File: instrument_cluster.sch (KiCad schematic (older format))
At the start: 2 parts

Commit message: finish scheme & change libs path
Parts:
- removed J?: Conn_02x16_Top_Bottom, symbol Conn_02x16_Top_Bottom
- added J1: Conn_02x16_Top_Bottom, Kulibin:Pin_Header_Angled_2x16_Pitch2.54mm, symbol Conn_02x16_Top_Bottom
- gave numbers to parts that had none: 1
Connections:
- net labels added: +3V3_A, +3V3_B, +5V_A, +5V_B, FUEL_TANK_in, FUEL_TANK_out1, FUEL_TANK_out2, LIN_(contact_spiral), LIN_+12V, USB_Vbus_A, USB_Vbus_B
- net labels removed: FUEL_TANK_in1, FUEL_TANK_in2, FUEL_TANK_out, SPIRAL
- wire segments 39 -> 78
- no-connect marks 2 -> 33
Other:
- note added: "two separate module on 1 PCB\n- module B powered from Vbatt\n- module A powered from IGN\n(Vbatt present always)"
- note removed: "two separate module on 1 PCB\n- module B power from Vbatt\n- module A power from IGN\n(Vbatt present always)"
- moved on the sheet: J2

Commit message: specify footpints to resistors and capasitors
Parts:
- J1: footprint Kulibin:Pin_Header_Angled_2x16_Pitch2.54mm -> zulljon:Pin_Header_Angled_2x16_Pitch2.54mm
- J2: footprint (none) -> zulljon:Socket_Strip_Straight_2x16_Pitch2.54mm
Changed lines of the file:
@@
 F 0 "J2" H 9500 2800 50  0000 C CNN
 F 1 "Conn_02x16_Top_Bottom" H 9500 1100 50  0000 C CNN
-F 2 "" H 9450 2000 50  0001 C CNN
+F 2 "zulljon:Socket_Strip_Straight_2x16_Pitch2.54mm" H 9450 2000 50  0001 C CNN
 F 3 "" H 9450 2000 50  0001 C CNN
 	1    9450 2000
@@
 	5750 3900 5750 4000
 $Comp
-L GND #PWR01
+L GND #PWR3
 U 1 1 5A075102
 P 5750 4000
-F 0 "#PWR01" H 5750 3750 50  0001 C CNN
+F 0 "#PWR3" H 5750 3750 50  0001 C CNN
 F 1 "GND" H 5750 3850 50  0000 C CNN
 F 2 "" H 5750 4000 50  0001 C CNN
@@
 $EndComp
 $Comp
-L GND #PWR02
+L GND #PWR1
 U 1 1 5A0766C2
 P 1000 7500
-F 0 "#PWR02" H 1000 7250 50  0001 C CNN
+F 0 "#PWR1" H 1000 7250 50  0001 C CNN
 F 1 "GND" H 1150 7450 50  0000 C CNN
 F 2 "" H 1000 7500 50  0001 C CNN
@@
 	5800 2350 5800 2450
 $Comp
-L GND #PWR03
+L GND #PWR4
 U 1 1 5A0B0A63
 P 5800 2450
-F 0 "#PWR03" H 5800 2200 50  0001 C CNN
+F 0 "#PWR4" H 5800 2200 50  0001 C CNN
 F 1 "GND" H 5800 2300 50  0000 C CNN
 F 2 "" H 5800 2450 50  0001 C CNN
@@
 	2250 3950 2250 4050
 $Comp
-L GND #PWR04
+L GND #PWR2
 U 1 1 5A0C0519
 P 2250 4050
-F 0 "#PWR04" H 2250 3800 50  0001 C CNN
+F 0 "#PWR2" H 2250 3800 50  0001 C CNN
 F 1 "GND" H 2250 3900 50  0000 C CNN
 F 2 "" H 2250 4050 50  0001 C CNN
@@
 F 0 "J1" H 2400 5450 50  0000 C CNN
 F 1 "Conn_02x16_Top_Bottom" H 2400 5550 50  0000 C CNN
-F 2 "Kulibin:Pin_Header_Angled_2x16_Pitch2.54mm" H 2350 6550 50  0001 C CNN
+F 2 "zulljon:Pin_Header_Angled_2x16_Pitch2.54mm" H 2350 6550 50  0001 C CNN
 F 3 "" H 2350 6550 50  0001 C CNN
 	1    2350 6550

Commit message: add missed footprints, add additional capasitors on 3.3V line, fix banch of ERC errors
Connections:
- no-connect marks 33 -> 34
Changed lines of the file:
@@
 	5750 3900 5750 4000
 $Comp
-L GND #PWR3
+L GND #PWR01
 U 1 1 5A075102
 P 5750 4000
-F 0 "#PWR3" H 5750 3750 50  0001 C CNN
+F 0 "#PWR01" H 5750 3750 50  0001 C CNN
 F 1 "GND" H 5750 3850 50  0000 C CNN
 F 2 "" H 5750 4000 50  0001 C CNN
@@
 $EndComp
 $Comp
-L GND #PWR1
+L GND #PWR02
 U 1 1 5A0766C2
-P 1000 7500
-F 0 "#PWR1" H 1000 7250 50  0001 C CNN
-F 1 "GND" H 1150 7450 50  0000 C CNN
-F 2 "" H 1000 7500 50  0001 C CNN
-F 3 "" H 1000 7500 50  0001 C CNN
-	1    1000 7500
+P 1300 7550
+F 0 "#PWR02" H 1300 7300 50  0001 C CNN
+F 1 "GND" H 1450 7500 50  0000 C CNN
+F 2 "" H 1300 7550 50  0001 C CNN
+F 3 "" H 1300 7550 50  0001 C CNN
+	1    1300 7550
 	1    0    0    -1
 $EndComp
@@
 	850  7400 950  7500
 Wire Wire Line
-	950  7500 1000 7500
+	950  7500 1300 7500
 Wire Bus Line
 	850  700  850  7400
@@
 	5800 2350 5800 2450
 $Comp
-L GND #PWR4
+L GND #PWR03
 U 1 1 5A0B0A63
 P 5800 2450
-F 0 "#PWR4" H 5800 2200 50  0001 C CNN
+F 0 "#PWR03" H 5800 2200 50  0001 C CNN
 F 1 "GND" H 5800 2300 50  0000 C CNN
 F 2 "" H 5800 2450 50  0001 C CNN
@@
 	2250 3950 2250 4050
 $Comp
-L GND #PWR2
+L GND #PWR04
 U 1 1 5A0C0519
 P 2250 4050
-F 0 "#PWR2" H 2250 3800 50  0001 C CNN
+F 0 "#PWR04" H 2250 3800 50  0001 C CNN
 F 1 "GND" H 2250 3900 50  0000 C CNN
 F 2 "" H 2250 4050 50  0001 C CNN
@@
 Wire Wire Line
 	9750 1600 10700 1600
+NoConn ~ 9750 1500
+Connection ~ 1300 7500
+Wire Wire Line
+	1300 7500 1300 7550
 $EndSCHEMATC

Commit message: delete LIN, fix ERC errors
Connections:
- no-connect marks 34 -> 35
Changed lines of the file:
@@
 F10 "USB_B" I L 5950 3700 59
 F11 "FUEL_ADC_POWER" O R 7450 3350 59
-F12 "LIN_+12V" O R 7450 3250 59
 $EndSheet
 $Sheet
@@
 F20 "BRAKE(fluid_level)" I L 2350 2650 60
 F21 "BELT_MINDER" I L 2350 2750 60
-F22 "LIN_+12V" I L 2350 3750 60
-F23 "LIN" B L 2350 2850 60
 $EndSheet
 Text Notes 7200 5900 0    118  ~ 0
@@
 	850  7400 950  7500
 Wire Wire Line
-	950  7500 1300 7500
+	950  7500 1550 7500
 Wire Bus Line
 	850  700  850  7400
@@
 	2350 3650 950  3650
 Wire Wire Line
-	2350 3750 950  3750
-Wire Wire Line
 	2350 3950 2250 3950
 Wire Wire Line
@@
 	850  3550 950  3650
 Entry Wire Line
-	850  3650 950  3750
-Entry Wire Line
 	5250 3500 5350 3600
 Entry Wire Line
 	5250 3600 5350 3700
-Text Label 1050 3750 0    60   ~ 0
-LIN_+12V
 Text Label 1050 3650 0    60   ~ 0
 USB_Vbus_B
 Text Label 5400 2250 0    60   ~ 0
 USB_Vbus_A
-Text Label 7550 3250 0    60   ~ 0
-LIN_+12V
 Text Label 7550 3550 0    60   ~ 0
 +3V3_A
@@
 Wire Wire Line
 	7450 3450 8200 3450
-Wire Wire Line
-	7450 3250 8200 3250
-Entry Wire Line
-	8200 3250 8300 3350
 Entry Wire Line
 	8200 3350 8300 3450
@@
 Text Label 1050 3550 0    60   ~ 0
 +3V3_B
-Text Label 1000 2850 0    60   ~ 0
-LIN_(contact_spiral)
-Entry Wire Line
-	850  2750 950  2850
-Wire Wire Line
-	950  2850 2350 2850
 Text Label 5350 3600 0    60   ~ 0
 USB_Vbus_A
@@
 Wire Wire Line
 	1300 7500 1300 7550
+NoConn ~ 9750 1600
+$Comp
+L PWR_FLAG #FLG05
+U 1 1 5A0F23B6
+P 1550 7500
+F 0 "#FLG05" H 1550 7575 50  0001 C CNN
+F 1 "PWR_FLAG" H 1550 7650 50  0000 C CNN
+F 2 "" H 1550 7500 50  0001 C CNN
+F 3 "" H 1550 7500 50  0001 C CNN
+	1    1550 7500
+	0    1    1    0
+$EndComp
 $EndSCHEMATC

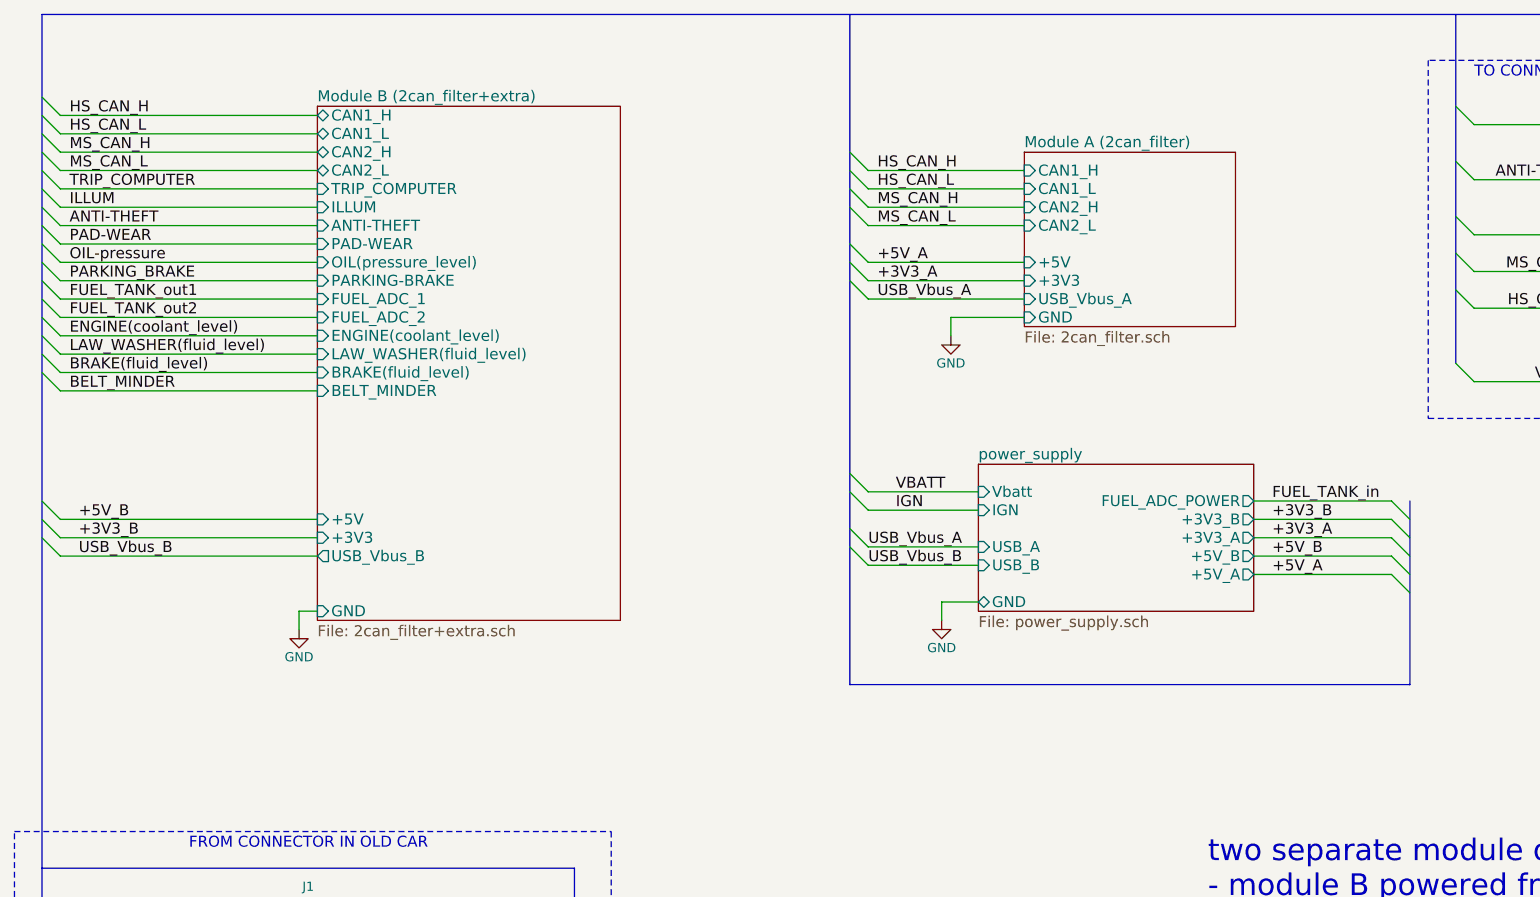
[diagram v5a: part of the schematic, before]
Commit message: redone shematic of power supply, fix usb_vbus and swd diods connections, change mcu capacitors connections
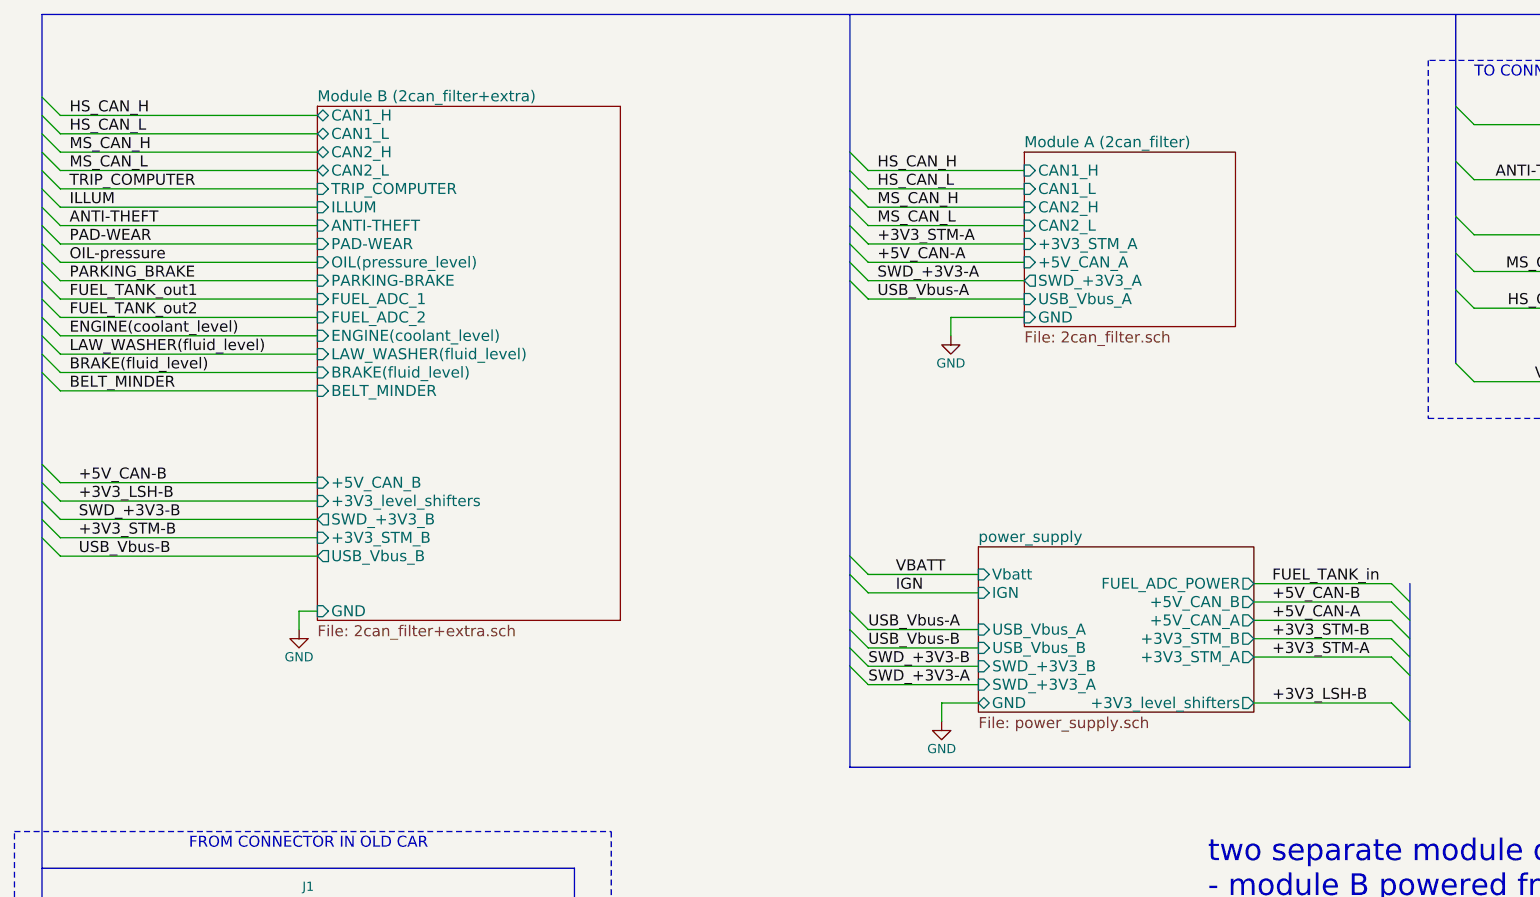
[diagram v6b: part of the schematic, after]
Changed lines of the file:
@@
 	10950 950  8400 950
-$Sheet
-S 5950 3150 1500 800
-U 5A047293
-F0 "power_supply" 60
-F1 "power_supply.sch" 60
-F2 "Vbatt" I L 5950 3300 59
-F3 "IGN" I L 5950 3400 59
-F4 "+3V3_A" O R 7450 3550 59
-F5 "+3V3_B" O R 7450 3450 59
-F6 "+5V_A" O R 7450 3750 59
-F7 "GND" B L 5950 3900 59
-F8 "+5V_B" O R 7450 3650 59
-F9 "USB_A" I L 5950 3600 59
-F10 "USB_B" I L 5950 3700 59
-F11 "FUEL_ADC_POWER" O R 7450 3350 59
-$EndSheet
 $Sheet
 S 6200 1450 1150 950
@@
 F0 "Module A (2can_filter)" 60
 F1 "2can_filter.sch" 60
-F2 "+3V3" I L 6200 2150 60
-F3 "CAN1_H" I L 6200 1550 60
-F4 "CAN1_L" I L 6200 1650 60
-F5 "CAN2_H" I L 6200 1750 60
-F6 "CAN2_L" I L 6200 1850 60
-F7 "GND" I L 6200 2350 60
-F8 "+5V" I L 6200 2050 60
-F9 "USB_Vbus_A" I L 6200 2250 60
+F2 "CAN1_H" I L 6200 1550 60
+F3 "CAN1_L" I L 6200 1650 60
+F4 "CAN2_H" I L 6200 1750 60
+F5 "CAN2_L" I L 6200 1850 60
+F6 "GND" I L 6200 2350 60
+F7 "USB_Vbus_A" I L 6200 2250 60
+F8 "+3V3_STM_A" I L 6200 1950 60
+F9 "+5V_CAN_A" I L 6200 2050 60
+F10 "SWD_+3V3_A" O L 6200 2150 60
 $EndSheet
 $Sheet
@@
 F0 "Module B (2can_filter+extra)" 60
 F1 "2can_filter+extra.sch" 60
-F2 "+3V3" I L 2350 3550 60
-F3 "GND" I L 2350 3950 60
-F4 "+5V" I L 2350 3450 60
-F5 "USB_Vbus_B" O L 2350 3650 60
-F6 "CAN1_H" B L 2350 1250 60
-F7 "CAN1_L" B L 2350 1350 60
-F8 "CAN2_H" B L 2350 1450 60
-F9 "CAN2_L" B L 2350 1550 60
-F10 "TRIP_COMPUTER" I L 2350 1650 60
-F11 "ILLUM" I L 2350 1750 60
-F12 "ANTI-THEFT" I L 2350 1850 60
-F13 "PAD-WEAR" I L 2350 1950 60
-F14 "OIL(pressure_level)" I L 2350 2050 60
-F15 "PARKING-BRAKE" I L 2350 2150 60
-F16 "FUEL_ADC_1" I L 2350 2250 60
-F17 "FUEL_ADC_2" I L 2350 2350 60
-F18 "ENGINE(coolant_level)" I L 2350 2450 60
-F19 "LAW_WASHER(fluid_level)" I L 2350 2550 60
-F20 "BRAKE(fluid_level)" I L 2350 2650 60
-F21 "BELT_MINDER" I L 2350 2750 60
+F2 "GND" I L 2350 3950 60
+F3 "USB_Vbus_B" O L 2350 3650 60
+F4 "CAN1_H" B L 2350 1250 60
+F5 "CAN1_L" B L 2350 1350 60
+F6 "CAN2_H" B L 2350 1450 60
+F7 "CAN2_L" B L 2350 1550 60
+F8 "TRIP_COMPUTER" I L 2350 1650 60
+F9 "ILLUM" I L 2350 1750 60
+F10 "ANTI-THEFT" I L 2350 1850 60
+F11 "PAD-WEAR" I L 2350 1950 60
+F12 "OIL(pressure_level)" I L 2350 2050 60
+F13 "PARKING-BRAKE" I L 2350 2150 60
+F14 "FUEL_ADC_1" I L 2350 2250 60
+F15 "FUEL_ADC_2" I L 2350 2350 60
+F16 "ENGINE(coolant_level)" I L 2350 2450 60
+F17 "LAW_WASHER(fluid_level)" I L 2350 2550 60
+F18 "BRAKE(fluid_level)" I L 2350 2650 60
+F19 "BELT_MINDER" I L 2350 2750 60
+F20 "+5V_CAN_B" I L 2350 3250 60
+F21 "+3V3_level_shifters" I L 2350 3350 60
+F22 "SWD_+3V3_B" O L 2350 3450 60
+F23 "+3V3_STM_B" I L 2350 3550 60
 $EndSheet
 Text Notes 7200 5900 0    118  ~ 0
 two separate module on 1 PCB\n- module B powered from Vbatt\n- module A powered from IGN\n(Vbatt present always)
 Wire Wire Line
-	5350 3300 5950 3300
-Wire Wire Line
-	5350 3400 5950 3400
-Wire Wire Line
-	5950 3600 5350 3600
-Wire Wire Line
-	5950 3700 5350 3700
-Wire Wire Line
-	5950 3900 5750 3900
-Wire Wire Line
-	5750 3900 5750 4000
+	5350 3750 5950 3750
+Wire Wire Line
+	5350 3850 5950 3850
+Wire Wire Line
+	5950 4050 5350 4050
+Wire Wire Line
+	5950 4150 5350 4150
+Wire Wire Line
+	5950 4450 5750 4450
+Wire Wire Line
+	5750 4450 5750 4550
 $Comp
 L GND #PWR01
 U 1 1 5A075102
-P 5750 4000
-F 0 "#PWR01" H 5750 3750 50  0001 C CNN
-F 1 "GND" H 5750 3850 50  0000 C CNN
-F 2 "" H 5750 4000 50  0001 C CNN
-F 3 "" H 5750 4000 50  0001 C CNN
-	1    5750 4000
+P 5750 4550
+F 0 "#PWR01" H 5750 4300 50  0001 C CNN
+F 1 "GND" H 5750 4400 50  0000 C CNN
+F 2 "" H 5750 4550 50  0001 C CNN
+F 3 "" H 5750 4550 50  0001 C CNN
+	1    5750 4550
 	1    0    0    -1
 $EndComp
@@
 $EndComp
 Wire Wire Line
-	7450 3350 8200 3350
-Text Label 7550 3350 0    60   ~ 0
+	7450 3800 8200 3800
+Text Label 7550 3800 0    60   ~ 0
 FUEL_TANK_in
 Entry Wire Line
@@
 Text Label 1000 1750 0    60   ~ 0
 ILLUM
-Text Label 5500 3300 0    60   ~ 0
+Text Label 5500 3750 0    60   ~ 0
 VBATT
-Text Label 5500 3400 0    60   ~ 0
+Text Label 5500 3850 0    60   ~ 0
 IGN
 Text Label 1000 1850 0    60   ~ 0
@@
 	850  2650 950  2750
 Entry Wire Line
-	5250 3200 5350 3300
+	5250 3650 5350 3750
 Wire Wire Line
 	950  2550 2350 2550
@@
 	950  2150 2350 2150
 Entry Wire Line
-	5250 3300 5350 3400
-Wire Bus Line
-	5250 700  5250 4350
+	5250 3750 5350 3850
+Wire Bus Line
+	5250 700  5250 4800
 Entry Wire Line
 	850  3450 950  3550
@@
 	850  3550 950  3650
 Entry Wire Line
-	5250 3500 5350 3600
-Entry Wire Line
-	5250 3600 5350 3700
+	5250 3950 5350 4050
+Entry Wire Line
+	5250 4050 5350 4150
 Text Label 1050 3650 0    60   ~ 0
-USB_Vbus_B
+USB_Vbus-B
 Text Label 5400 2250 0    60   ~ 0
-USB_Vbus_A
-Text Label 7550 3550 0    60   ~ 0
-+3V3_A
-Text Label 7550 3450 0    60   ~ 0
-+3V3_B
-Text Label 7550 3750 0    60   ~ 0
-+5V_A
-Text Label 7550 3650 0    60   ~ 0
-+5V_B
-Wire Wire Line
-	7450 3750 8200 3750
-Wire Wire Line
-	7450 3650 8200 3650
-Wire Wire Line
-	7450 3550 8200 3550
-Wire Wire Line
-	7450 3450 8200 3450
-Entry Wire Line
-	8200 3350 8300 3450
-Entry Wire Line
-	8200 3450 8300 3550
-Entry Wire Line
-	8200 3550 8300 3650
-Entry Wire Line
-	8200 3650 8300 3750
-Entry Wire Line
-	8200 3750 8300 3850
-Wire Bus Line
-	8300 3350 8300 4350
-Wire Bus Line
-	8300 4350 5250 4350
+USB_Vbus-A
+Wire Wire Line
+	7450 4200 8200 4200
+Wire Wire Line
+	7450 4100 8200 4100
+Wire Wire Line
+	7450 4000 8200 4000
+Wire Wire Line
+	7450 3900 8200 3900
+Entry Wire Line
+	8200 3800 8300 3900
+Entry Wire Line
+	8200 3900 8300 4000
+Entry Wire Line
+	8200 4000 8300 4100
+Entry Wire Line
+	8200 4100 8300 4200
+Entry Wire Line
+	8200 4200 8300 4300
+Wire Bus Line
+	8300 3800 8300 4800
+Wire Bus Line
+	8300 4800 5250 4800
 Text Label 5400 2050 0    60   ~ 0
-+5V_A
++5V_CAN-A
 Text Label 5400 2150 0    60   ~ 0
-+3V3_A
+SWD_+3V3-A
 Entry Wire Line
 	5250 1950 5350 2050
@@
 	5350 2150 6200 2150
 Text Label 1050 3450 0    60   ~ 0
-+5V_B
+SWD_+3V3-B
 Text Label 1050 3550 0    60   ~ 0
-+3V3_B
-Text Label 5350 3600 0    60   ~ 0
-USB_Vbus_A
-Text Label 5350 3700 0    60   ~ 0
-USB_Vbus_B
++3V3_STM-B
+Text Label 5350 4050 0    60   ~ 0
+USB_Vbus-A
+Text Label 5350 4150 0    60   ~ 0
+USB_Vbus-B
 $Comp
 L Conn_02x16_Top_Bottom J1
@@
 	0    1    1    0
 $EndComp
+Wire Wire Line
+	6200 1950 5350 1950
+Entry Wire Line
+	5250 1850 5350 1950
+Text Label 5400 1950 0    60   ~ 0
++3V3_STM-A
+Wire Wire Line
+	2350 3250 950  3250
+Wire Wire Line
+	950  3350 2350 3350
+Entry Wire Line
+	850  3150 950  3250
+Entry Wire Line
+	850  3250 950  3350
+Text Label 1050 3250 0    60   ~ 0
++5V_CAN-B
+Text Label 1050 3350 0    60   ~ 0
++3V3_LSH-B
+$Sheet
+S 5950 3600 1500 900
+U 5A047293
+F0 "power_supply" 60
+F1 "power_supply.sch" 60
+F2 "Vbatt" I L 5950 3750 59
+F3 "IGN" I L 5950 3850 59
+F4 "GND" B L 5950 4450 59
+F5 "FUEL_ADC_POWER" O R 7450 3800 59
+F6 "+3V3_STM_A" O R 7450 4200 60
+F7 "+3V3_STM_B" O R 7450 4100 60
+F8 "+5V_CAN_B" O R 7450 3900 60
+F9 "+5V_CAN_A" O R 7450 4000 60
+F10 "USB_Vbus_B" I L 5950 4150 60
+F11 "+3V3_level_shifters" O R 7450 4450 60
+F12 "USB_Vbus_A" I L 5950 4050 60
+F13 "SWD_+3V3_B" I L 5950 4250 60
+F14 "SWD_+3V3_A" I L 5950 4350 60
+$EndSheet
+Wire Wire Line
+	7450 4450 8200 4450
+Entry Wire Line
+	8200 4450 8300 4550
+Text Label 7550 3900 0    60   ~ 0
++5V_CAN-B
+Text Label 7550 4000 0    60   ~ 0
++5V_CAN-A
+Text Label 5350 4250 0    60   ~ 0
+SWD_+3V3-B
+Text Label 5350 4350 0    60   ~ 0
+SWD_+3V3-A
+Text Label 7550 4450 0    60   ~ 0
++3V3_LSH-B
+Wire Wire Line
+	5950 4250 5350 4250
+Wire Wire Line
+	5350 4350 5950 4350
+Entry Wire Line
+	5250 4250 5350 4350
+Entry Wire Line
+	5250 4150 5350 4250
+Text Label 7550 4200 0    60   ~ 0
++3V3_STM-A
+Text Label 7550 4100 0    60   ~ 0
++3V3_STM-B
 $EndSCHEMATC

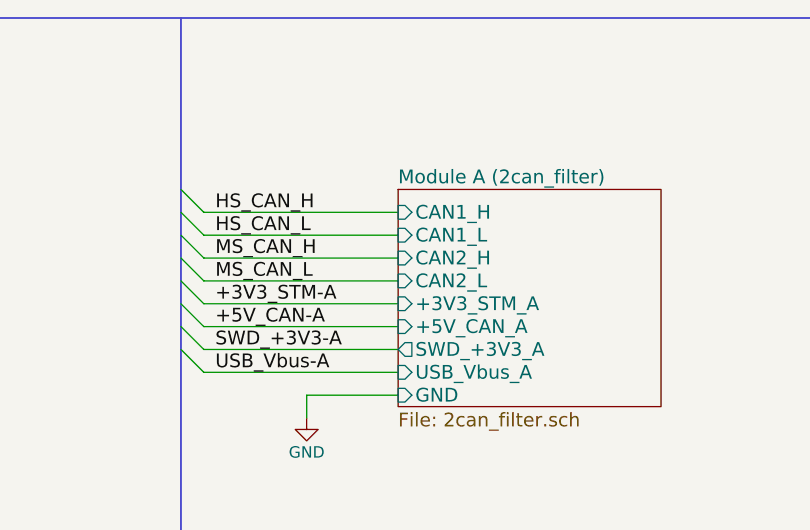
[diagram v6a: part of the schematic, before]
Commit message: add transient voltage suppression diods on CAN
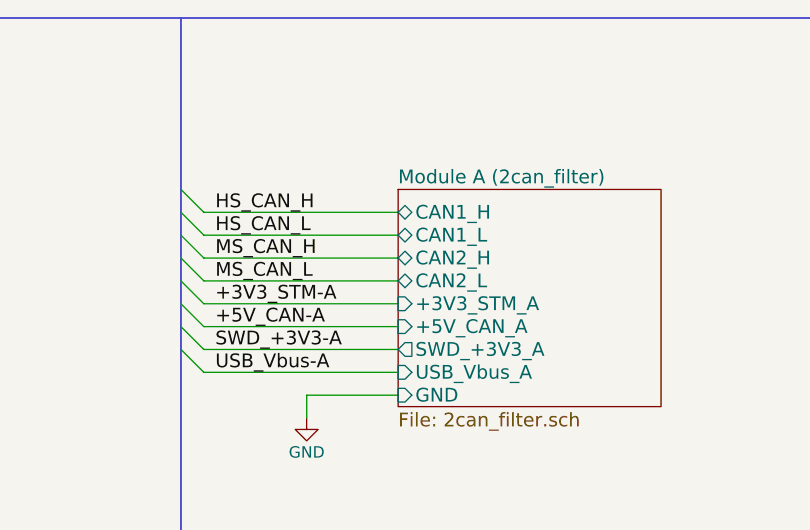
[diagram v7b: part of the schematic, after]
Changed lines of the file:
@@
 F0 "Module A (2can_filter)" 60
 F1 "2can_filter.sch" 60
-F2 "CAN1_H" I L 6200 1550 60
-F3 "CAN1_L" I L 6200 1650 60
-F4 "CAN2_H" I L 6200 1750 60
-F5 "CAN2_L" I L 6200 1850 60
+F2 "CAN1_H" B L 6200 1550 60
+F3 "CAN1_L" B L 6200 1650 60
+F4 "CAN2_H" B L 6200 1750 60
+F5 "CAN2_L" B L 6200 1850 60
 F6 "GND" I L 6200 2350 60
 F7 "USB_Vbus_A" I L 6200 2250 60
